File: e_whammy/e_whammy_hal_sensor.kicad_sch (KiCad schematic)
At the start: 9 parts, among them J1 I/O connector, U1 HT7550-1, U2 DRV5056

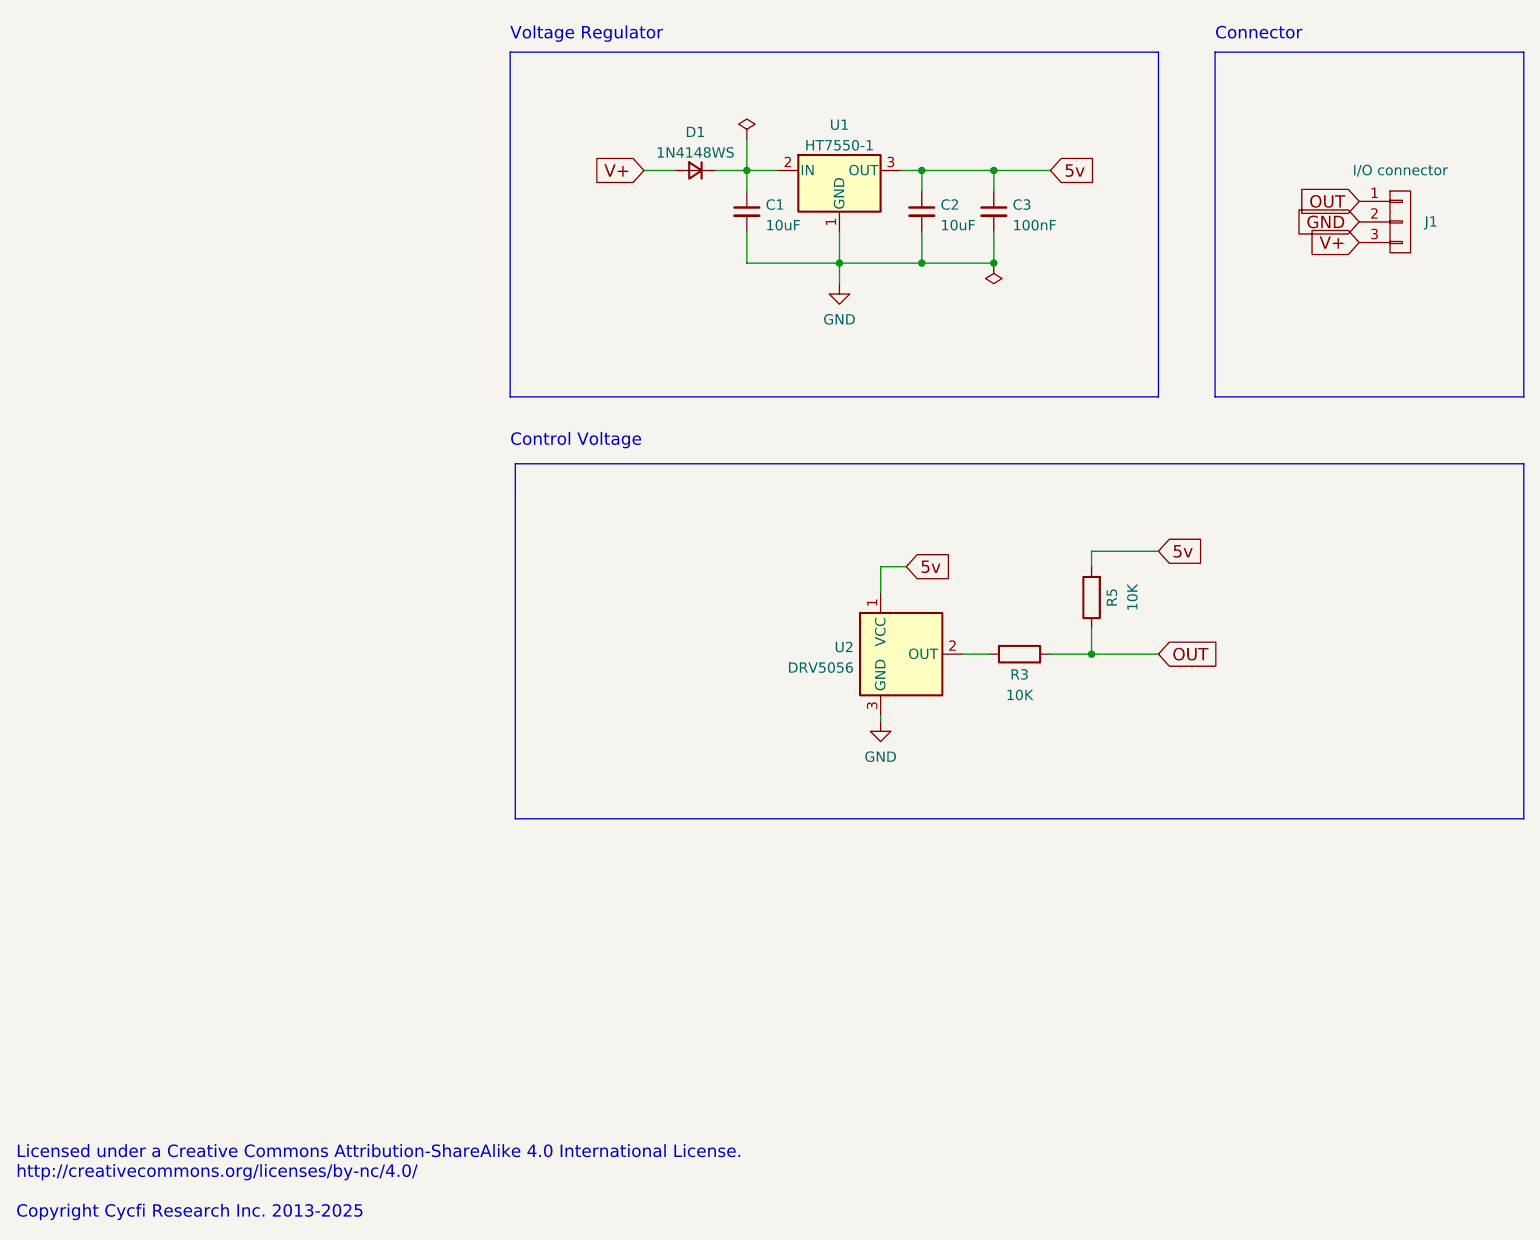
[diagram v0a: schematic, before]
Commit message: Separate the HAL sensor from CV conditioning
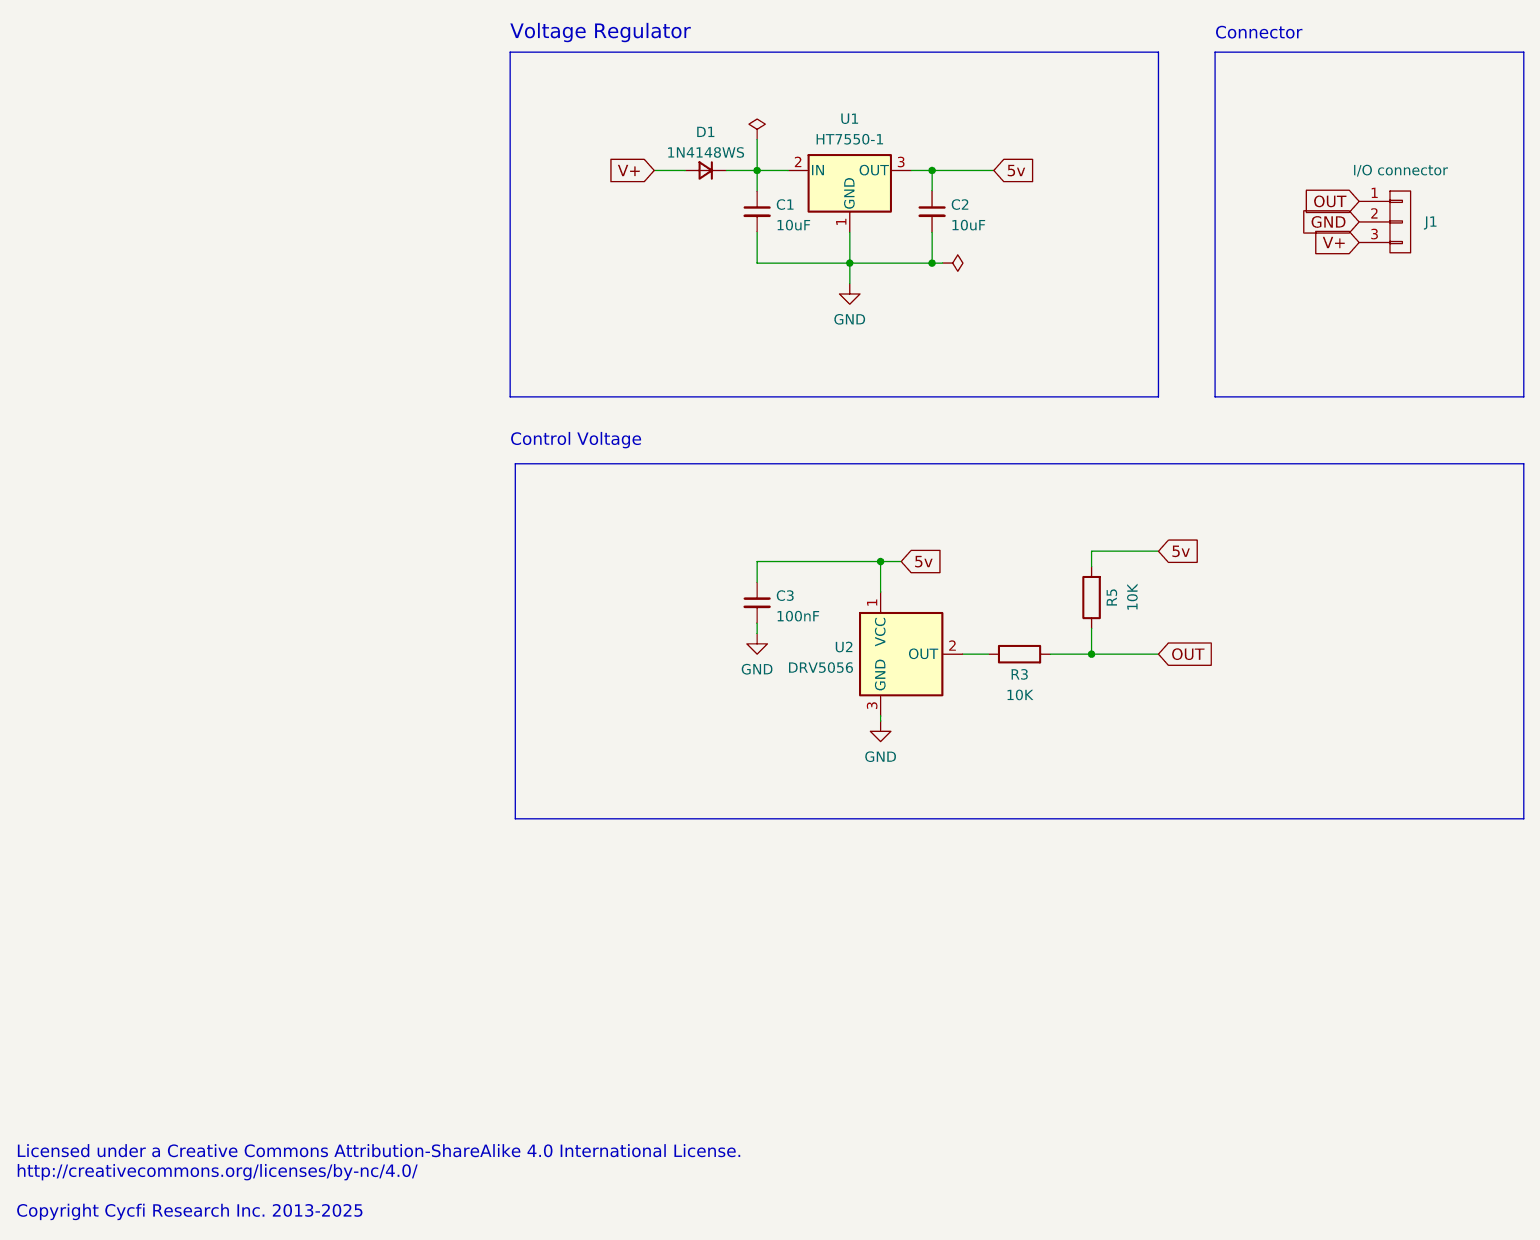
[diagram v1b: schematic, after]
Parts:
- U1: symbol cycfi_library:sot89-3-gio -> cycfi_library:fixed_voltage_regulator_gio
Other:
- moved on the sheet: C1, C2, C3, D1, U1
